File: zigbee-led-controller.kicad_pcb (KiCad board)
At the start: 2 copper layers, 10.7 x 18.3 mm, 60 parts, among them J1 SWD Header, J2 UART, J3 12V_Input, J4 LED_Connector, J5 5V_Input, J6 USB_B_Micro, Q1 IRLML0040TRPbF, Q2 IRLML0040TRPbF, Q3 IRLML0040TRPbF, Q4 IRLML0040TRPbF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

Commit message: PCB Initial placement
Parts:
- added J7: 2.1x5.5mm, Library:GRAVITECH_CON-SOCJ-2155, F.Cu at (43.2, 61.0)
- J1, J2: footprint Connector_PinHeader_2.54mm:PinHeader_1x02_P2.54mm_Horizontal -> Connector_PinHeader_2.54mm:PinHeader_1x02_P2.54mm_Vertical
- J3: footprint Connector_Molex:Molex_KK-396_A-41792-0004_1x04_P3.96mm_Horizontal -> Connector_PinHeader_2.54mm:PinHeader_1x04_P2.54mm_Horizontal
- J4: footprint Connector_PinHeader_2.54mm:PinHeader_1x03_P2.54mm_Vertical -> Connector_PinHeader_2.54mm:PinHeader_1x05_P2.54mm_Vertical
- J5: footprint Connector_Molex:Molex_KK-396_A-41792-0002_1x02_P3.96mm_Horizontal -> Connector_PinHeader_2.54mm:PinHeader_1x02_P2.54mm_Horizontal
- moved J2 78.9 mm to (94.0, 38.3), turned to 90 degrees
- moved R5 78.3 mm to (114.2, 46.0), turned to 180 degrees
- moved R10 77.0 mm to (117.7, 57.4), turned to 180 degrees
- moved R12 77.0 mm to (117.6, 63.0), turned to 180 degrees
- moved R6 76.8 mm to (117.6, 46.0), turned to 180 degrees
- moved R8 76.8 mm to (117.5, 51.7), turned to 180 degrees
- moved Q4 76.7 mm to (110.2, 62.0)
- moved Q3 76.3 mm to (110.3, 56.4)
- moved Q2 75.7 mm to (110.1, 50.7)
- moved J4 75.5 mm to (124.1, 44.7)
- moved Q1 75.4 mm to (110.2, 45.0)
- moved R9 73.8 mm to (114.2, 57.4), turned to 180 degrees
- moved R11 73.8 mm to (114.2, 63.0), turned to 180 degrees
- moved R7 73.6 mm to (114.1, 51.7), turned to 180 degrees
- moved JP6 72.7 mm to (114.2, 60.8)
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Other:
- board size 10.7 x 18.3 mm -> 92.8 x 35.1 mm
- rule pad_to_mask_clearance: 0 -> 0.075

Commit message: Routing done, first pass anyway.
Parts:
- moved J1 30.8 mm to (81.8, 64.8), turned to -90 degrees
- moved SW1 4.33 mm to (74.2, 62.2), turned to -90 degrees
- moved J2 2.64 mm to (93.2, 35.8)
- moved JP8 1.89 mm to (47.5, 35.6), turned to 0 degrees
- moved JP2 1.27 mm to (120.0, 36.1)
- moved TP5 0.77 mm to (83.8, 35.6)
- turned D2 to 90 degrees
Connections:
- U2 pad 1: /R_LED_d -> /WP
- U2 pad 2: /G_LED_d -> /W_LED_d
- U2 pad 3: /WP -> /B_LED_d
- U2 pad 4: /B_LED_d -> /G_LED_d
- U2 pad 9: /W_LED_d -> /R_LED_d
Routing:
- net +5V: track 0.00 -> 125.5 mm, vias 0 -> 4
- net +12V: track 0.00 -> 91.2 mm
- net GND: track 0.00 -> 58.7 mm, vias 0 -> 13
- net /SCL: track 0.00 -> 49.0 mm, vias 0 -> 2
- net /WP: track 0.00 -> 43.0 mm
- net /SDA: track 0.00 -> 39.0 mm, vias 0 -> 2
- net +5VD: track 0.00 -> 29.2 mm, vias 0 -> 2
- net /G_LED_d: track 0.00 -> 28.1 mm
- net /TX: track 0.00 -> 26.7 mm, vias 0 -> 2
- net /B_LED_d: track 0.00 -> 26.1 mm
- net /W_LED_d: track 0.00 -> 25.6 mm
- net /SWCLK: track 0.00 -> 21.7 mm, vias 0 -> 1
- net /SWDIO: track 0.00 -> 20.9 mm, vias 0 -> 1
- net /R_LED_d: track 0.00 -> 19.3 mm
- net +3V3: track 0.00 -> 13.5 mm, vias 0 -> 5
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- added copper zone on F.Cu, net +12V
- added copper zone on B.Cu, net +3V3
- added copper zone on F.Cu, net /V_LED
- added copper zone on B.Cu, net GND

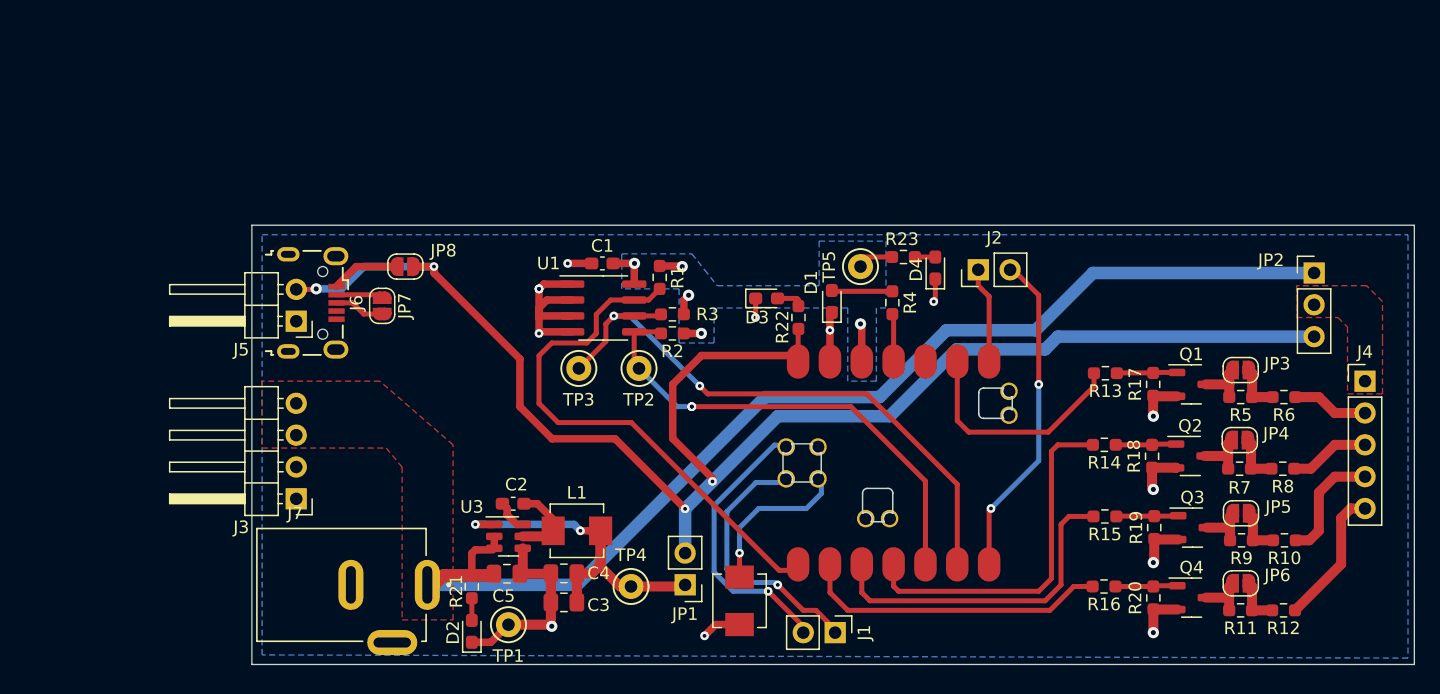
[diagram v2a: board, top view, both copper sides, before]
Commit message: Updated some footprints and finalized layout. Added better output connector and rst switch
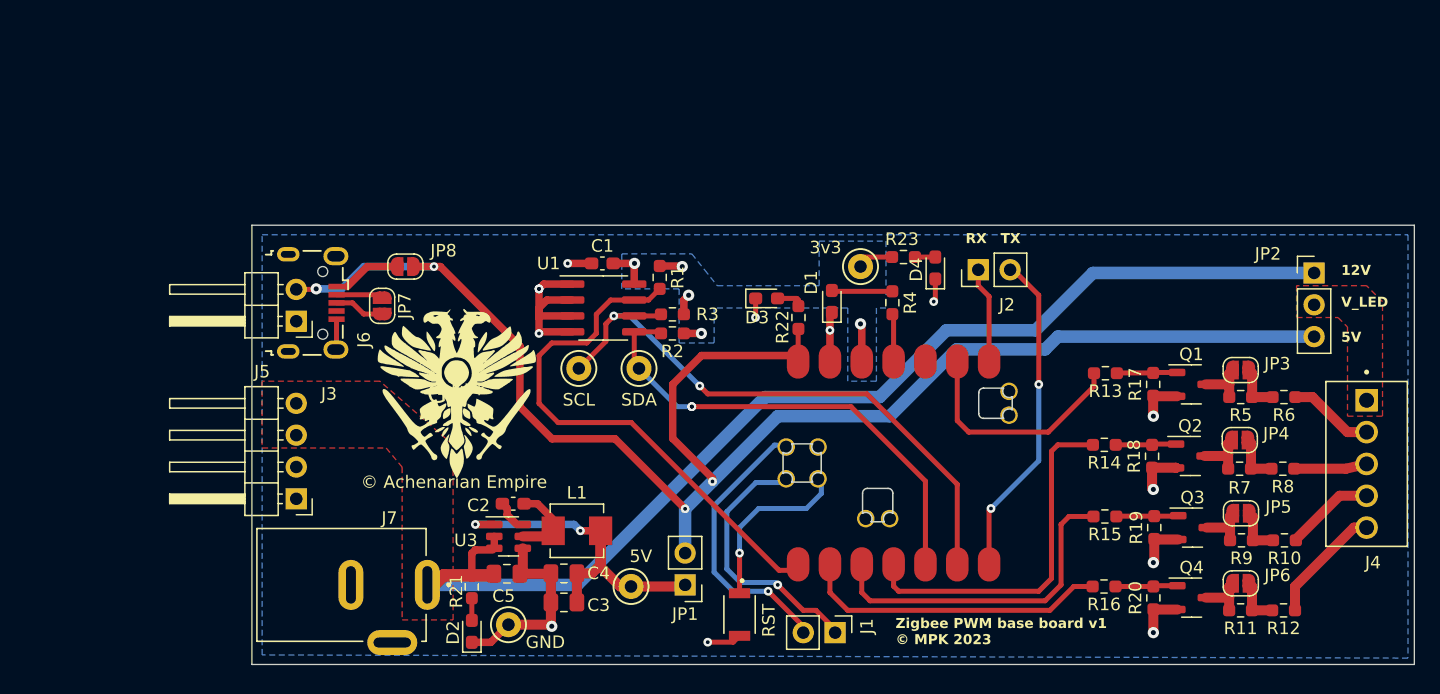
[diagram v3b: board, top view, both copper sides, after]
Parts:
- added G***: LOGO, Library:logo, F.Cu at (51.6, 45.7)
- J4: footprint Connector_PinHeader_2.54mm:PinHeader_1x05_P2.54mm_Vertical -> Library:TE_282834-5
- RST: renamed from SW1; footprint Inductor_SMD:L_Vishay_IHLP-1616 -> Library:SW_B3U-1000P
- moved J4 6.61 mm to (124.2, 51.3), turned to -90 degrees
- moved RST 1.09 mm to (74.2, 63.3)
- turned 3v3 to 0 degrees
- renumbered TP5 to 3v3, TP4 to 5V, TP1 to GND, TP3 to SCL, TP2 to SDA
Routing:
- net Net-(J4-Pin_4): track 9.41 -> 7.16 mm
- net GND: track 58.7 -> 60.7 mm
- net Net-(J4-Pin_5): track 11.1 -> 9.57 mm
- net /RESETn: track 12.2 -> 13.5 mm
- net Net-(J4-Pin_2): track 6.08 -> 6.84 mm
- net Net-(J4-Pin_3): track 6.43 -> 5.81 mm
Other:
- rule pad_to_mask_clearance: 0.075 -> 0
- board text added: "12V"
- board text added: "5V"
- board text added: "RX"
- board text added: "TX"
- board text added: "V_LED"
- board text added: "Zigbee PWM base board v1 © MPK 2023"

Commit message: Updated, given to pcbway to quote
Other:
- board text added: "GND"
- board text added: "SWCLK"
- board text added: "SWDIO"
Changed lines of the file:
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@@
     (property "Sheetname" "")
     (attr smd)
-    (fp_text reference "RST" (at 0.475 -2.335 90) (layer "F.SilkS")
+    (fp_text reference "RST" (at 1.192 2.794 -180) (layer "F.SilkS")
         (effects (font (size 1 1) (thickness 0.15)))
     )
@@
     (property "ki_keywords" "connector")
     (attr through_hole)
-    (fp_text reference "J3" (at -2.6089 8.372) (layer "F.SilkS")
+    (fp_text reference "J3" (at -2.6089 8.372) (layer "F.SilkS") hide
         (effects (font (size 1 1) (thickness 0.15)))
     )
@@
     (property "ki_keywords" "Jumper SPST")
     (attr through_hole)
-    (fp_text reference "JP1" (at 0 -2.33) (layer "F.SilkS")
+    (fp_text reference "JP1" (at -0.0254 4.826) (layer "F.SilkS")
         (effects (font (size 1 1) (thickness 0.15)))
     )
@@
     (property "ki_keywords" "connector")
     (attr through_hole)
-    (fp_text reference "J1" (at -0.508 -2.535 90) (layer "F.SilkS")
+    (fp_text reference "J1" (at -0.508 -2.535 90) (layer "F.SilkS") hide
         (effects (font (size 1 1) (thickness 0.15)))
     )
@@
     (effects (font (size 0.8 0.8) (thickness 0.15) bold) (justify left bottom))
   )
+  (gr_text "SWDIO" (at 84.582 66.294 90) (layer "F.SilkS")
+    (effects (font (size 0.8 0.8) (thickness 0.15) bold) (justify left bottom))
+  )
+  (gr_text "12V" (at 41.91 48.514 90) (layer "F.SilkS")
+    (effects (font (size 0.8 0.8) (thickness 0.15) bold) (justify left bottom))
+  )
   (gr_text "5V" (at 122.174 41.656) (layer "F.SilkS")
     (effects (font (size 0.8 0.8) (thickness 0.15) bold) (justify left bottom))
@@
     (effects (font (size 0.8 0.8) (thickness 0.15) bold) (justify left bottom))
   )
+  (gr_text "GND" (at 41.91 54.102 90) (layer "F.SilkS")
+    (effects (font (size 0.8 0.8) (thickness 0.15) bold) (justify left bottom))
+  )
   (gr_text "12V" (at 122.174 36.322) (layer "F.SilkS")
     (effects (font (size 0.8 0.8) (thickness 0.15) bold) (justify left bottom))
@@
     (effects (font (size 0.8 0.8) (thickness 0.15) bold) (justify left bottom))
   )
+  (gr_text "SWCLK" (at 77.216 66.802 90) (layer "F.SilkS")
+    (effects (font (size 1 1) (thickness 0.15)) (justify left bottom))
+  )
   (dimension (type aligned) (layer "Dwgs.User")
